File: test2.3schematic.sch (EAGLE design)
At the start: 24 parts, among them IC1 NCS21911SN2T1G, IC2 FXLN8371QR1, IC3 MAX25210ATAB9_V+, IC4 NCS21911SN2T1G, IC5 NCS21911SN2T1G

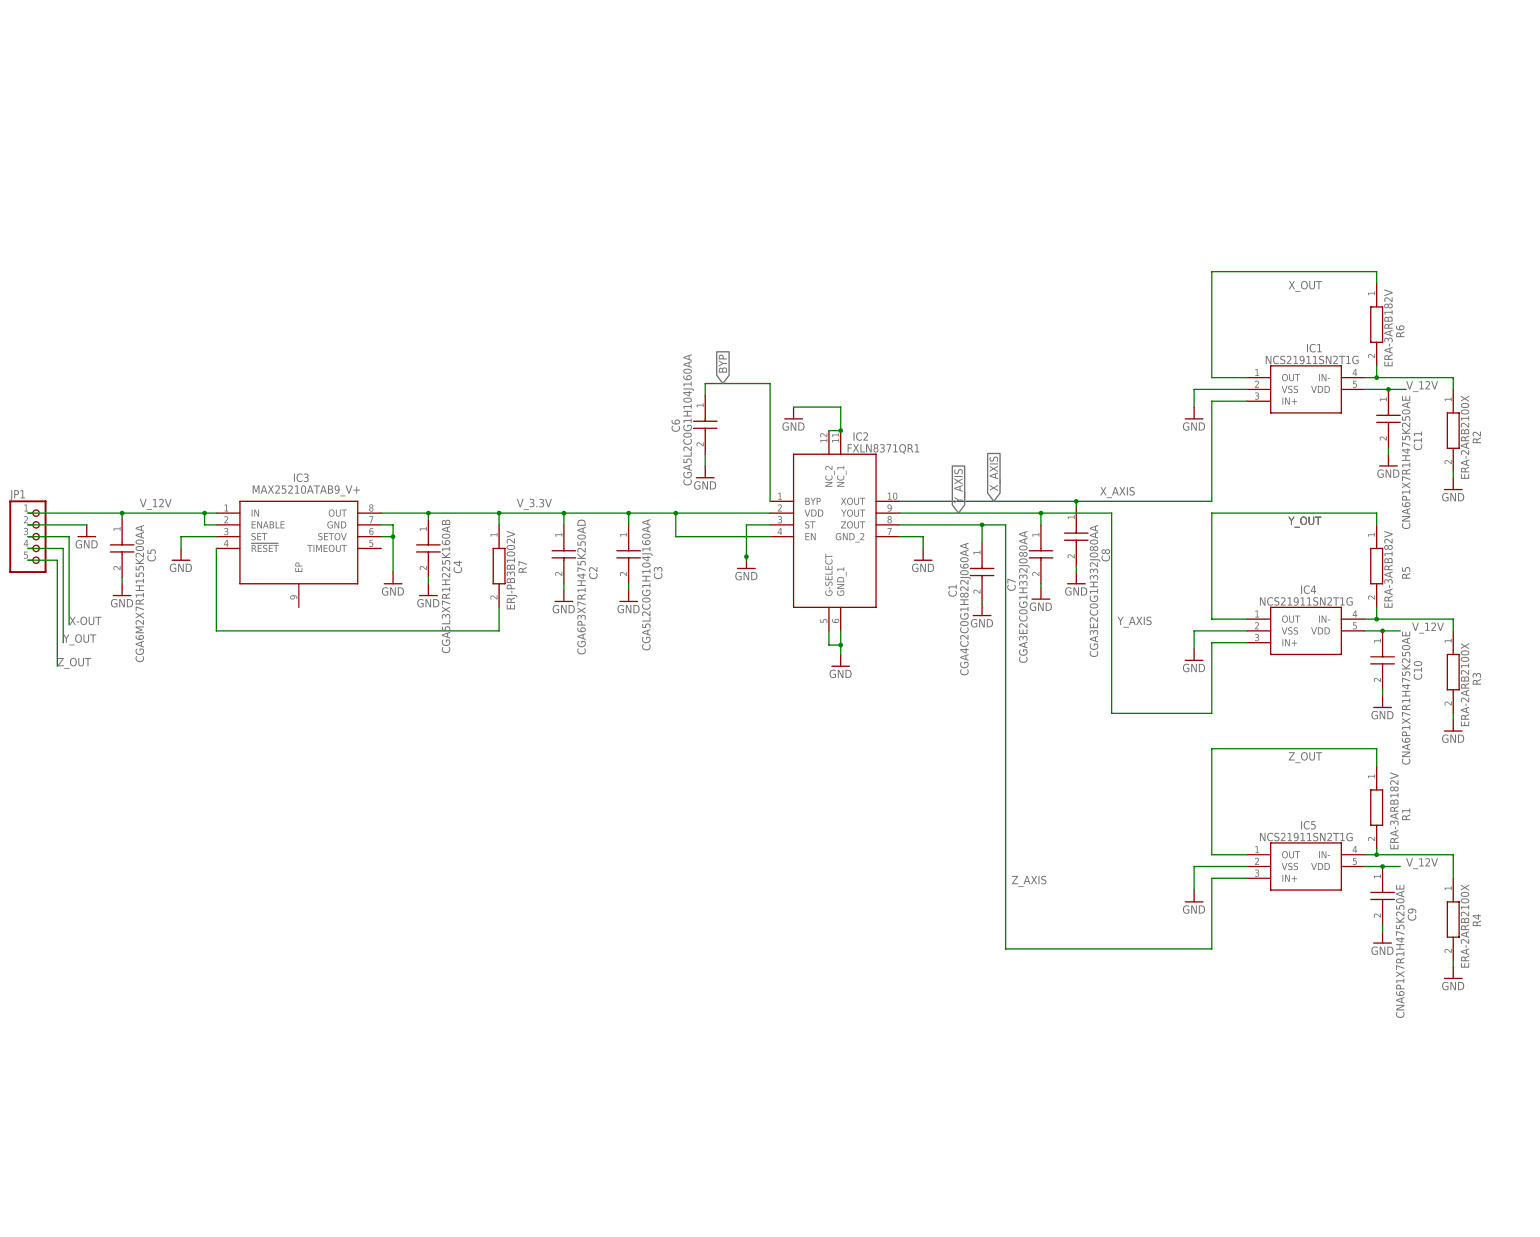
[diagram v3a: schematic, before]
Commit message: Finished The 8G_Accelerometer, awaiting review from FOrrest FOr final revision
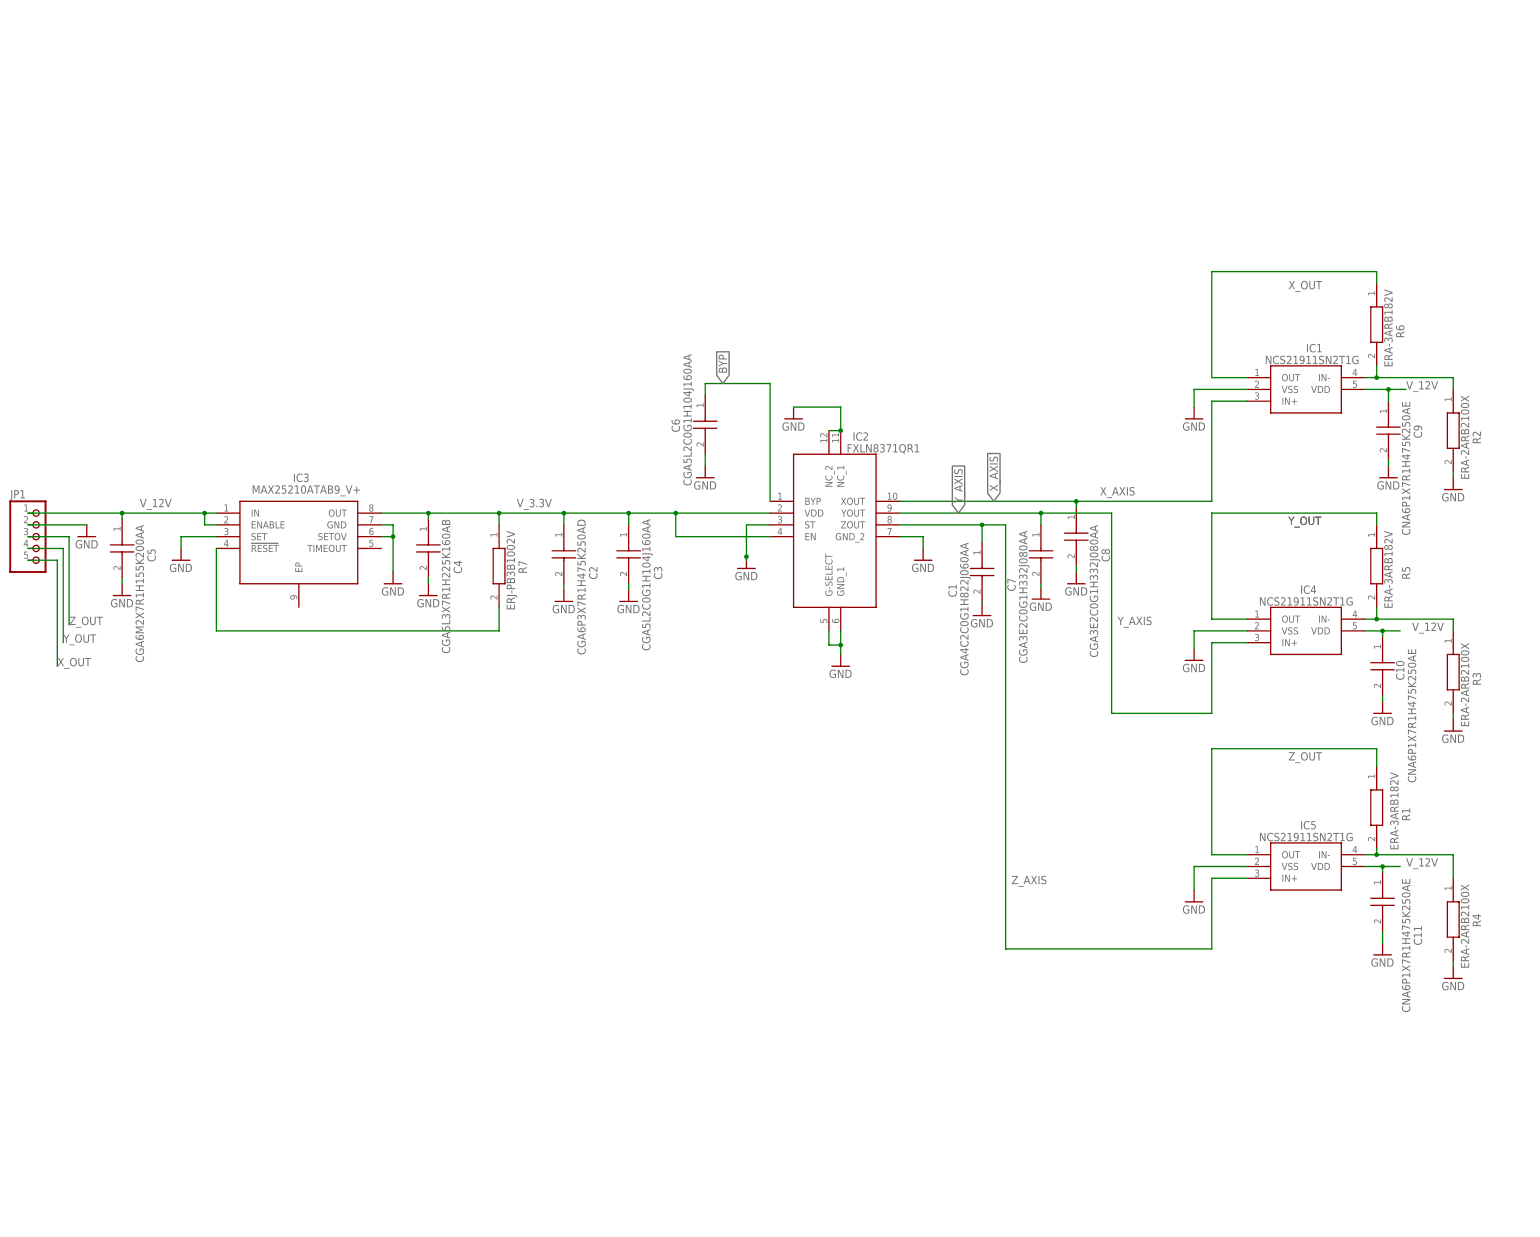
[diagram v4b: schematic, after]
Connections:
- removed net X-OUT: JP1.3
- net X_OUT: now also JP1.5
- net Z_OUT: now also JP1.3; no longer JP1.5
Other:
- moved on the sheet: C10, C11, C9

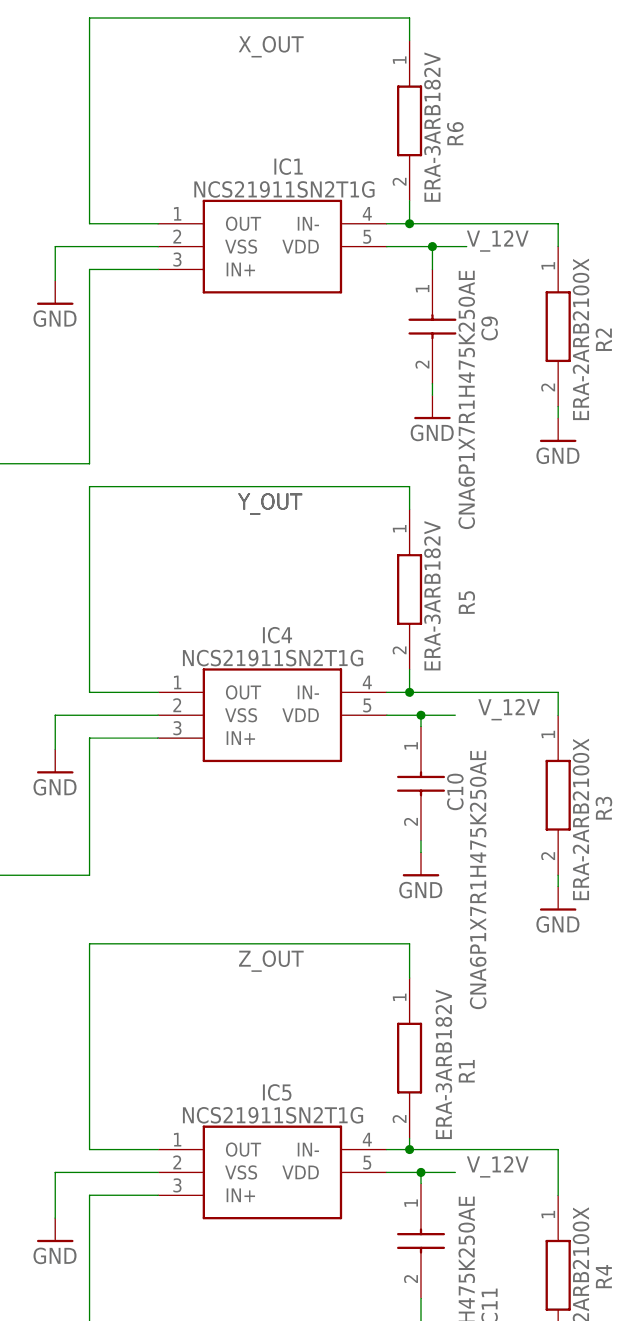
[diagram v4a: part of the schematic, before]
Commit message: Just 2 airwires left to connect, waiting for Forrest Review
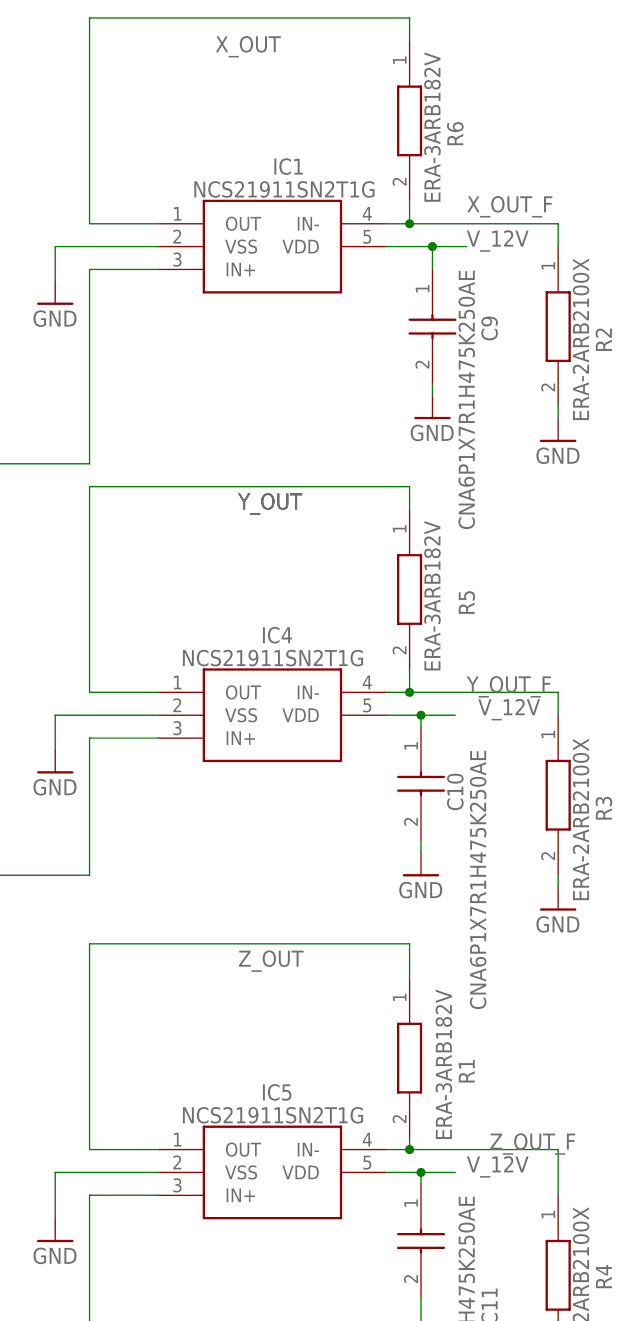
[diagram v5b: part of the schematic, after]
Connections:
- new net X_OUT_F: IC1.IN-, R2.1, R6.2
- new net Y_OUT_F: IC4.IN-, R3.1, R5.2
- new net Z_OUT_F: IC5.IN-, R1.2, R4.1
- net X_OUT: no longer IC1.IN-, R2.1, R6.2
- net Y_OUT: no longer IC4.IN-, R3.1, R5.2
- net Z_OUT: no longer IC5.IN-, R1.2, R4.1
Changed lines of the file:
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@@
 <net name="X_OUT" class="0">
-<segment>
-<wire x1="173.99" y1="29.21" x2="176.53" y2="29.21" width="0.1524" layer="91"/>
-<wire x1="176.53" y1="29.21" x2="193.04" y2="29.21" width="0.1524" layer="91"/>
-<wire x1="193.04" y1="29.21" x2="193.04" y2="26.67" width="0.1524" layer="91"/>
-<wire x1="176.53" y1="29.21" x2="176.53" y2="31.75" width="0.1524" layer="91"/>
-<junction x="176.53" y="29.21"/>
-<pinref part="R6" gate="G$1" pin="2"/>
-<pinref part="R2" gate="G$1" pin="1"/>
-<pinref part="IC1" gate="G$1" pin="IN-"/>
-</segment>
 <segment>
 <wire x1="148.59" y1="29.21" x2="140.97" y2="29.21" width="0.1524" layer="91"/>
@@
 <wire x1="176.53" y1="52.07" x2="140.97" y2="52.07" width="0.1524" layer="91"/>
 <wire x1="140.97" y1="52.07" x2="140.97" y2="29.21" width="0.1524" layer="91"/>
-<label x="157.48" y="48.26" size="1.778" layer="95"/>
+<label x="154.94" y="48.26" size="1.778" layer="95"/>
 <pinref part="R6" gate="G$1" pin="1"/>
 <pinref part="IC1" gate="G$1" pin="OUT"/>
@@
 </segment>
 <segment>
-<wire x1="173.99" y1="-22.86" x2="176.53" y2="-22.86" width="0.1524" layer="91"/>
-<wire x1="176.53" y1="-20.32" x2="176.53" y2="-22.86" width="0.1524" layer="91"/>
-<junction x="176.53" y="-22.86"/>
-<wire x1="176.53" y1="-22.86" x2="193.04" y2="-22.86" width="0.1524" layer="91"/>
-<wire x1="193.04" y1="-22.86" x2="193.04" y2="-25.4" width="0.1524" layer="91"/>
-<pinref part="R5" gate="G$1" pin="2"/>
-<pinref part="R3" gate="G$1" pin="1"/>
-<pinref part="IC4" gate="G$1" pin="IN-"/>
-</segment>
-<segment>
 <wire x1="148.59" y1="-22.86" x2="140.97" y2="-22.86" width="0.1524" layer="91"/>
 <wire x1="140.97" y1="-22.86" x2="140.97" y2="0" width="0.1524" layer="91"/>
@@
 </net>
 <net name="Z_OUT" class="0">
-<segment>
-<wire x1="173.99" y1="-73.66" x2="176.53" y2="-73.66" width="0.1524" layer="91"/>
-<wire x1="176.53" y1="-73.66" x2="193.04" y2="-73.66" width="0.1524" layer="91"/>
-<wire x1="193.04" y1="-73.66" x2="193.04" y2="-78.74" width="0.1524" layer="91"/>
-<wire x1="176.53" y1="-72.39" x2="176.53" y2="-73.66" width="0.1524" layer="91"/>
-<junction x="176.53" y="-73.66"/>
-<pinref part="R1" gate="G$1" pin="2"/>
-<pinref part="R4" gate="G$1" pin="1"/>
-<pinref part="IC5" gate="G$1" pin="IN-"/>
-</segment>
 <segment>
 <wire x1="148.59" y1="-73.66" x2="140.97" y2="-73.66" width="0.1524" layer="91"/>
@@
 </segment>
 </net>
+<net name="X_OUT_F" class="0">
+<segment>
+<wire x1="173.99" y1="29.21" x2="176.53" y2="29.21" width="0.1524" layer="91"/>
+<wire x1="176.53" y1="29.21" x2="193.04" y2="29.21" width="0.1524" layer="91"/>
+<wire x1="193.04" y1="29.21" x2="193.04" y2="26.67" width="0.1524" layer="91"/>
+<wire x1="176.53" y1="29.21" x2="176.53" y2="31.75" width="0.1524" layer="91"/>
+<junction x="176.53" y="29.21"/>
+<pinref part="R6" gate="G$1" pin="2"/>
+<pinref part="R2" gate="G$1" pin="1"/>
+<pinref part="IC1" gate="G$1" pin="IN-"/>
+<label x="182.88" y="30.48" size="1.778" layer="95"/>
+</segment>
+</net>
+<net name="Y_OUT_F" class="0">
+<segment>
+<wire x1="173.99" y1="-22.86" x2="176.53" y2="-22.86" width="0.1524" layer="91"/>
+<wire x1="176.53" y1="-20.32" x2="176.53" y2="-22.86" width="0.1524" layer="91"/>
+<junction x="176.53" y="-22.86"/>
+<wire x1="176.53" y1="-22.86" x2="193.04" y2="-22.86" width="0.1524" layer="91"/>
+<wire x1="193.04" y1="-22.86" x2="193.04" y2="-25.4" width="0.1524" layer="91"/>
+<pinref part="R5" gate="G$1" pin="2"/>
+<pinref part="R3" gate="G$1" pin="1"/>
+<pinref part="IC4" gate="G$1" pin="IN-"/>
+<label x="182.88" y="-22.86" size="1.778" layer="95"/>
+</segment>
+</net>
+<net name="Z_OUT_F" class="0">
+<segment>
+<wire x1="173.99" y1="-73.66" x2="176.53" y2="-73.66" width="0.1524" layer="91"/>
+<wire x1="176.53" y1="-73.66" x2="193.04" y2="-73.66" width="0.1524" layer="91"/>
+<wire x1="193.04" y1="-73.66" x2="193.04" y2="-78.74" width="0.1524" layer="91"/>
+<wire x1="176.53" y1="-72.39" x2="176.53" y2="-73.66" width="0.1524" layer="91"/>
+<junction x="176.53" y="-73.66"/>
+<pinref part="R1" gate="G$1" pin="2"/>
+<pinref part="R4" gate="G$1" pin="1"/>
+<pinref part="IC5" gate="G$1" pin="IN-"/>
+<label x="185.42" y="-73.66" size="1.778" layer="95"/>
+</segment>
+</net>
 </nets>
 </sheet>
 </sheets>
+<errors>
+</errors>
 </schematic>
 </drawing>

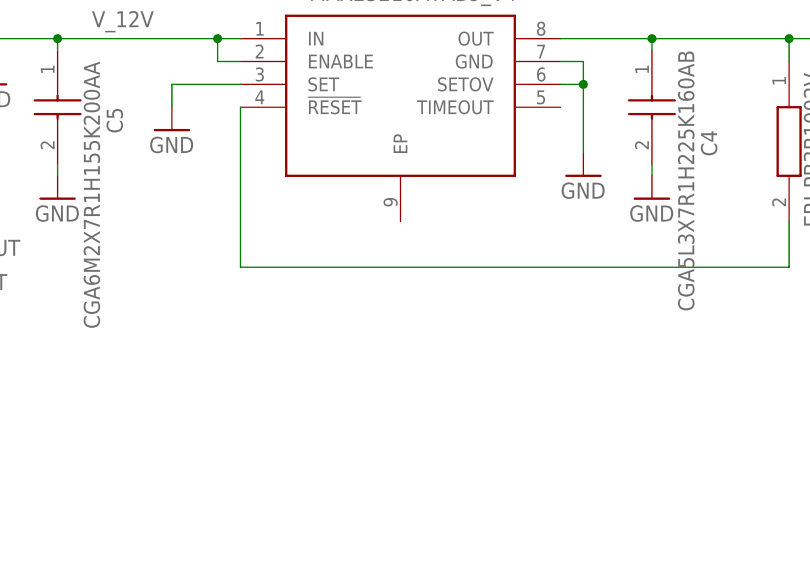
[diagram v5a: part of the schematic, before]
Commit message: NO errors Everything done and connected, PCB Design has been completed now waiting for Forrest's Review, if HE approves then done if not this is just a draft
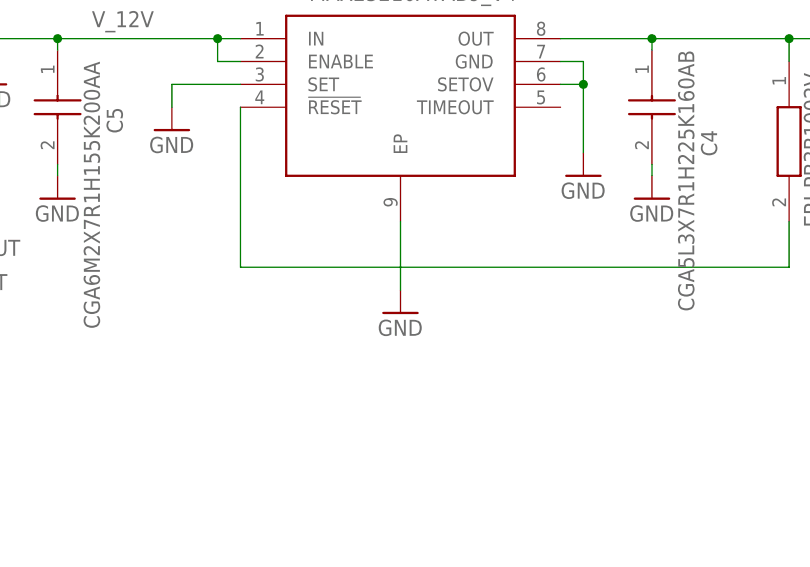
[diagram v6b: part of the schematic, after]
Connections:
- net GND: now also IC3.EP
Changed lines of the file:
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@@
 <part name="C10" library="SamacSys_Parts" library_urn="urn:adsk.eagle:library:32027058" deviceset="CNA6P1X7R1H475K250AE" device="" package3d_urn="urn:adsk.eagle:package:31985600/2"/>
 <part name="C11" library="SamacSys_Parts" library_urn="urn:adsk.eagle:library:32027058" deviceset="CNA6P1X7R1H475K250AE" device="" package3d_urn="urn:adsk.eagle:package:31985600/2"/>
+<part name="GND25" library="supply1" library_urn="urn:adsk.eagle:library:371" deviceset="GND" device=""/>
 </parts>
 <sheets>
@@
 <attribute name="VALUE" x="182.88" y="-78.74" size="1.778" layer="96" rot="R270" align="center-left"/>
 </instance>
+<instance part="GND25" gate="1" x="-55.88" y="-30.48" smashed="yes">
+<attribute name="VALUE" x="-58.42" y="-33.02" size="1.778" layer="96"/>
+</instance>
 </instances>
 <busses>
@@
 <wire x1="40.64" y1="-2.54" x2="45.72" y2="-2.54" width="0.1524" layer="91"/>
 </segment>
+<segment>
+<pinref part="IC3" gate="G$1" pin="EP"/>
+<pinref part="GND25" gate="1" pin="GND"/>
+<wire x1="-55.88" y1="-20.32" x2="-55.88" y2="-27.94" width="0.1524" layer="91"/>
+</segment>
 </net>
